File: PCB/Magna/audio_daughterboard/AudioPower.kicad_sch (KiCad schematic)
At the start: 54 parts, among them U901 TLV61046ADBVR, U902 TLV76701DRVx, U903 TLV76701DRVx, U904 TLV76701DRVx

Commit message: "Finalize" Audio daugherboard
Finished DAC output filter
Fixed the whole damn MCU subschematic
Fixed Linedriver schematic
Added component footprints and LCSC numbers
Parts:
- removed R901: 680R, Resistor_SMD:R_0805_2012Metric_Pad1.20x1.40mm_HandSolder, symbol Device:R_Small
- removed R904: 1k, Resistor_SMD:R_0805_2012Metric_Pad1.20x1.40mm_HandSolder, symbol Device:R_Small
- removed R911, R912: 470, Resistor_SMD:R_0805_2012Metric_Pad1.20x1.40mm_HandSolder, symbol Device:R_Small
- removed R913: 680, Resistor_SMD:R_0805_2012Metric_Pad1.20x1.40mm_HandSolder, symbol Device:R_Small
- removed U902, U903, U904: TLV76701DRVx, Package_SON:WSON-6-1EP_2x2mm_P0.65mm_EP1x1.6mm_ThermalVias, symbol Regulator_Linear:TLV76701DRVx
- added C904, C905, C906: 10uF, Capacitor_SMD:CP_Elec_4x5.8, symbol Device:C_Polarized
- added R901, R920: 680R, Resistor_SMD:R_0603_1608Metric, symbol Device:R
- added R904, R921: 2k15, Resistor_SMD:R_0603_1608Metric, symbol Device:R
- added R907, R911, R913: 22k, Resistor_SMD:R_0603_1608Metric, symbol Device:R
- added R912, R915: 10k, Resistor_SMD:R_0603_1608Metric, symbol Device:R
- added R914, R918: 100k, Resistor_SMD:R_0603_1608Metric, symbol Device:R
- added R916: 4k7, Resistor_SMD:R_0603_1608Metric, symbol Device:R
- added R919: 348R, Resistor_SMD:R_0603_1608Metric, symbol Device:R
- added TP902: TestPoint, TestPoint:TestPoint_Keystone_5005-5009_Compact, symbol Connector:TestPoint
- added U902, U903, U904: LM350_TO263-3, Package_TO_SOT_SMD:TO-263-3_TabPin2, symbol Regulator_Linear:LM350_TO220
- C901, C903, FB901, FB902, FB903, FB904, FB905, L901, R902, TP901, V901, V902: now left out of the parts list
- C902: footprint Capacitor_SMD:C_0805_2012Metric_Pad1.18x1.45mm_HandSolder -> Capacitor_SMD:C_0603_1608Metric; LCSC C1804 -> C1653; now left out of the parts list
- C907: renamed from C904; now left out of the parts list
- C908: renamed from C905; now left out of the parts list
- C909: renamed from C906; now left out of the parts list
- C910: renamed from C908; footprint (none) -> Capacitor_SMD:C_0603_1608Metric; LCSC (none) -> C1653; now left out of the parts list
- C911: renamed from C909; footprint (none) -> Capacitor_SMD:C_0603_1608Metric; LCSC (none) -> C1653; now left out of the parts list
- C912: renamed from C907; footprint (none) -> Capacitor_SMD:C_0603_1608Metric; LCSC (none) -> C1653; now left out of the parts list
- C913: renamed from C910; now left out of the parts list
- C914: renamed from C911; now left out of the parts list
- C915: renamed from C912; now left out of the parts list
- C916: renamed from C913; footprint Capacitor_SMD:CP_Elec_5x5.8 -> Skrooter_footprints:c_elec_SMD_12.5x13.5; symbol Device:C_Polarized -> Device:C; LCSC C2163245 -> C3829328; now left out of the parts list
- C917: renamed from C914; footprint Capacitor_SMD:CP_Elec_5x5.8 -> Skrooter_footprints:c_elec_SMD_12.5x13.5; symbol Device:C_Polarized -> Device:C; LCSC C2163245 -> C3829328; now left out of the parts list
- C918: renamed from C915; footprint Capacitor_SMD:CP_Elec_5x5.8 -> Skrooter_footprints:c_elec_SMD_12.5x13.5; symbol Device:C_Polarized -> Device:C; LCSC C2163245 -> C3829328; now left out of the parts list
- C919: renamed from C916; now left out of the parts list
- C920: renamed from C917; now left out of the parts list
- C921: renamed from C918; now left out of the parts list
- D901, D902, D903, D904, D905: footprint Diode_SMD:D_0805_2012Metric_Pad1.15x1.40mm_HandSolder -> LED_SMD:LED_0805_2012Metric; now left out of the parts list
- R903: footprint Resistor_SMD:R_0805_2012Metric_Pad1.20x1.40mm_HandSolder -> Resistor_SMD:R_0603_1608Metric; LCSC C149504 -> C95204; now left out of the parts list
- R905: value 499k -> 100k; footprint (none) -> Resistor_SMD:R_0603_1608Metric; LCSC (none) -> C25803; now left out of the parts list
- R906: value 160k -> 10k; footprint (none) -> Resistor_SMD:R_0603_1608Metric; LCSC (none) -> C95204; now left out of the parts list
- R908: value 33k -> 4k7; footprint (none) -> Resistor_SMD:R_0603_1608Metric; LCSC (none) -> C2989582; now left out of the parts list
- R909: value 160k -> 22k; footprint (none) -> Resistor_SMD:R_0603_1608Metric; LCSC (none) -> C335085; now left out of the parts list
- R910: value 15k -> 100k; footprint (none) -> Resistor_SMD:R_0603_1608Metric; LCSC (none) -> C25803; now left out of the parts list
- R917: renamed from R907; footprint (none) -> Resistor_SMD:R_0603_1608Metric; LCSC (none) -> C25803; now left out of the parts list
- TP903: renamed from TP902; now left out of the parts list
- TP904: renamed from TP903; now left out of the parts list
- TP905: renamed from TP904; now left out of the parts list
- TP906: renamed from TP905; now left out of the parts list
- TP907: renamed from TP906; now left out of the parts list
- U901: LCSC (none) -> C464815
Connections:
- net +5V: now also R901.2
- net 16V: now also C904.1, C905.1, C906.1, R904.2
- net Boost in: now also U902.3 (VI)
- net GND: now also C904.2, C905.2, C906.2, R913.2, R914.2, R916.1, R918.2, TP902.1; no longer R906.2, R908.2
- net 14.5VAA: now reaches C911.1, C915.1, C918.1, FB905.1
- net 14.5VAA: now also R905.1, R921.2, U904.2 (VO); no longer R909.1
- net at C910.1, C914.1, C917.1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: now also R920.2, U903.2 (VO)
- net at C910.2, R917.2: now also R910.1, R914.1, R918.1, U903.1 (ADJ); no longer R908.1
- net at C912.1, C913.1, C916.1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: now also R906.1, R919.2, U902.2 (VO); no longer R905.1
- net at C908.1, C909.1, FB902.2: now also U903.3 (VI), U904.3 (VI)
- net at D901.2 (A): now also R901.1
- net at D905.2 (A): now also R921.1
- net at D904.2 (A): now also R920.1
- net at D902.2 (A): now also R904.1
- net at D903.2 (A): now also R919.1
- new net: R905.2, R907.2
- new net: C912.2, R911.2, R913.1, U902.1 (ADJ)
- new net: R907.1, R909.2
- new net: C911.2, R912.2, R915.1, U904.1 (ADJ)
- new net: R909.1, R912.1
- new net: R915.2, R916.2
- new net: R906.2, R908.2
- new net: R908.1, R911.1
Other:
- note added: "Should be 36k over 22k"
- moved on the sheet: C902, C903, C907, C908, C909, C910, C911, C912, C913, C914, C915, C919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

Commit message: Do most of the component placement for audio board
Just a general layout, things will probably change
as the routing begins.
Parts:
- removed C905: 10uF, Capacitor_SMD:CP_Elec_4x5.8, symbol Device:C_Polarized
- removed C907, C913, C919: 4.7uF, Capacitor_SMD:C_0805_2012Metric_Pad1.18x1.45mm_HandSolder, symbol Device:C
- removed C912: 22pF, Capacitor_SMD:C_0603_1608Metric, symbol Device:C
- removed C916, C917, C918: 22uF, Skrooter_footprints:c_elec_SMD_12.5x13.5, symbol Device:C
- removed D903: Red, LED_SMD:LED_0805_2012Metric, symbol Device:LED_Small
- removed FB903: FerriteBead, Inductor_SMD:L_0805_2012Metric, symbol Device:FerriteBead
- removed R906: 10k, Resistor_SMD:R_0603_1608Metric, symbol Device:R
- removed R908: 4k7, Resistor_SMD:R_0603_1608Metric, symbol Device:R
- removed R911, R913: 22k, Resistor_SMD:R_0603_1608Metric, symbol Device:R
- removed R919: 348R, Resistor_SMD:R_0603_1608Metric, symbol Device:R
- removed TP901, TP904, TP905: TestPoint, TestPoint:TestPoint_Keystone_5005-5009_Compact, symbol Connector:TestPoint
- removed U902: LM350_TO263-3, Package_TO_SOT_SMD:TO-263-3_TabPin2, symbol Regulator_Linear:LM350_TO220
- added C913, C914, C917: 220uF, Capacitor_SMD:CP_Elec_4x5.8, symbol Device:C_Polarized
- added FB902: FerriteBead, Inductor_SMD:L_0805_2012Metric, symbol Device:FerriteBead
- added R903: 22k, Resistor_SMD:R_0603_1608Metric, symbol Device:R
- added TP1: TestPoint, TestPoint:TestPoint_Pad_1.0x1.0mm, symbol Connector:TestPoint_Alt
- added TP906, TP908: TestPoint, TestPoint:TestPoint_Keystone_5005-5009_Compact, symbol Connector:TestPoint
- C901, C903: footprint Capacitor_SMD:C_0805_2012Metric_Pad1.18x1.45mm_HandSolder -> Capacitor_SMD:C_1206_3216Metric; LCSC C1779 -> C29823
- C907: renamed from C908; footprint Capacitor_SMD:C_0805_2012Metric_Pad1.18x1.45mm_HandSolder -> Capacitor_SMD:C_1206_3216Metric; LCSC C1779 -> C29823
- C908: renamed from C909; footprint Capacitor_SMD:C_0805_2012Metric_Pad1.18x1.45mm_HandSolder -> Capacitor_SMD:C_1206_3216Metric; LCSC C1779 -> C29823
- C911: renamed from C914; footprint Capacitor_SMD:C_0805_2012Metric_Pad1.18x1.45mm_HandSolder -> Capacitor_SMD:C_1206_3216Metric; LCSC C1779 -> C29823
- C912: renamed from C915; footprint Capacitor_SMD:C_0805_2012Metric_Pad1.18x1.45mm_HandSolder -> Capacitor_SMD:C_1206_3216Metric; LCSC C1779 -> C29823
- C915: renamed from C920; footprint Capacitor_SMD:C_0805_2012Metric_Pad1.18x1.45mm_HandSolder -> Capacitor_SMD:C_1206_3216Metric; LCSC C1779 -> C29823
- C916: renamed from C921; footprint Capacitor_SMD:C_0805_2012Metric_Pad1.18x1.45mm_HandSolder -> Capacitor_SMD:C_1206_3216Metric; LCSC C1779 -> C29823
- R902: value 120k -> 100k; footprint Resistor_SMD:R_0805_2012Metric_Pad1.20x1.40mm_HandSolder -> Resistor_SMD:R_0603_1608Metric; LCSC C17709 -> C25803
- renumbered C910 to C909, C911 to C910, D904 to D903, D905 to D904, FB902 to FB903, R903 to R904, R904 to R905, R905 to R906, R910 to R907, R907 to R908, R914 to R910, R912 to R911, R917 to R912, R918 to R913, R915 to R914, R916 to R915, R920 to R916, R921 to R917, TP907 to TP905, TP906 to TP907, U903 to U902, U904 to U903
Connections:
- net +5VA: no longer TP907.1
- net 14.5VAA: now also TP905.1, C914.1
- net 16V: now also C917.1, FB902.1
- net Boost Feedback: now also R903.1; no longer R902.2
- net Boost_SW: now also TP1.1
- net GND: now also C913.2, C914.2, C917.2, TP906.1, TP908.1
- net VAA: no longer TP905.1
- net 5VA_PRE_FERRITE: now reaches C909.1, C911.1, FB904.1, R912.1, R916.2, U902.2 (VO)
- net 5VA_PRE_FERRITE: now also TP907.1, C913.1
- net at C908.1, FB903.2, U903.3 (VI): no longer C907.1, U902.3 (VI)
- net 14.5VAA_FEEDBACK: now reaches C910.2, R911.2, R914.1, U903.1 (ADJ)
- new net: R902.2, R903.2
- new net: C907.1, FB902.2, U902.3 (VI)
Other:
- note removed: "3.3V/250mA"
- note removed: "Should be 36k over 22k"
- moved on the sheet: C904, C907, C908, C909, C910, C911, C912, C915, C916, D903, D904, FB904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

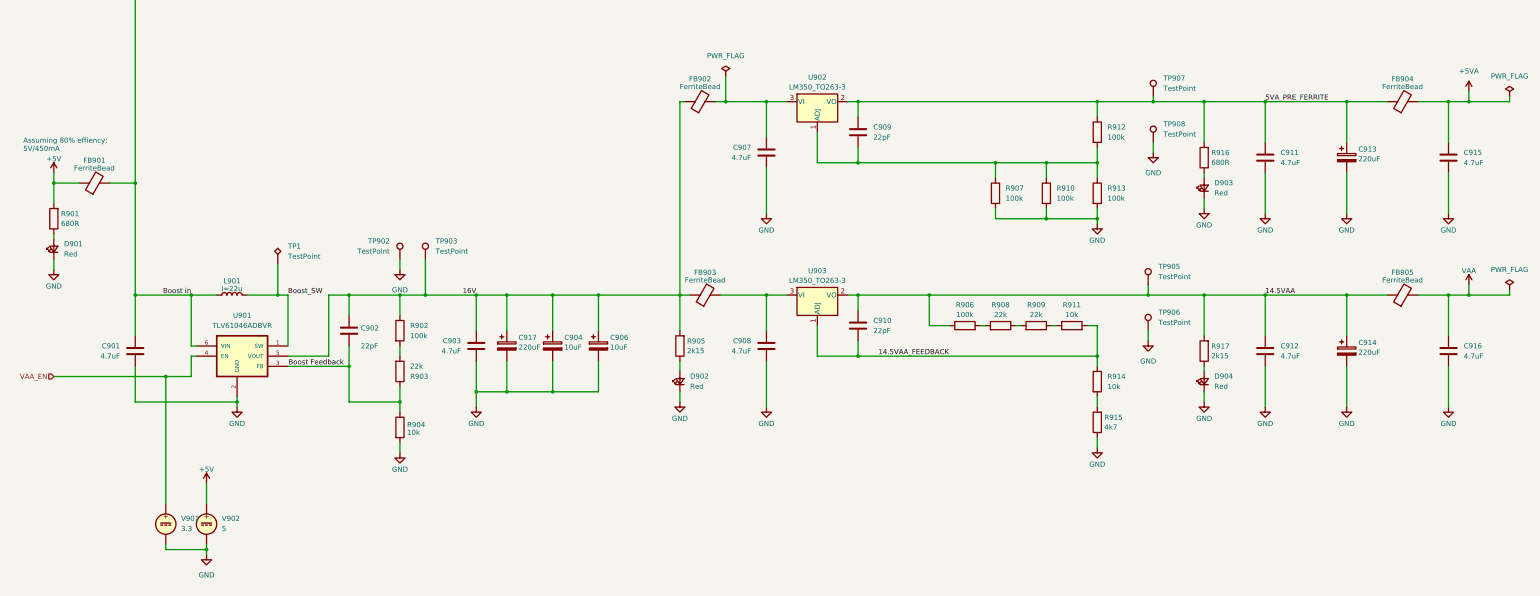
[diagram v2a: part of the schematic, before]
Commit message: Start layout and routing of Audio Daugherboard
Also a lot of small changes to everything that became apperant
when the audio daughterboard was designed. Such as the Headphone
PCB, which is now separate from the rest of the audio.
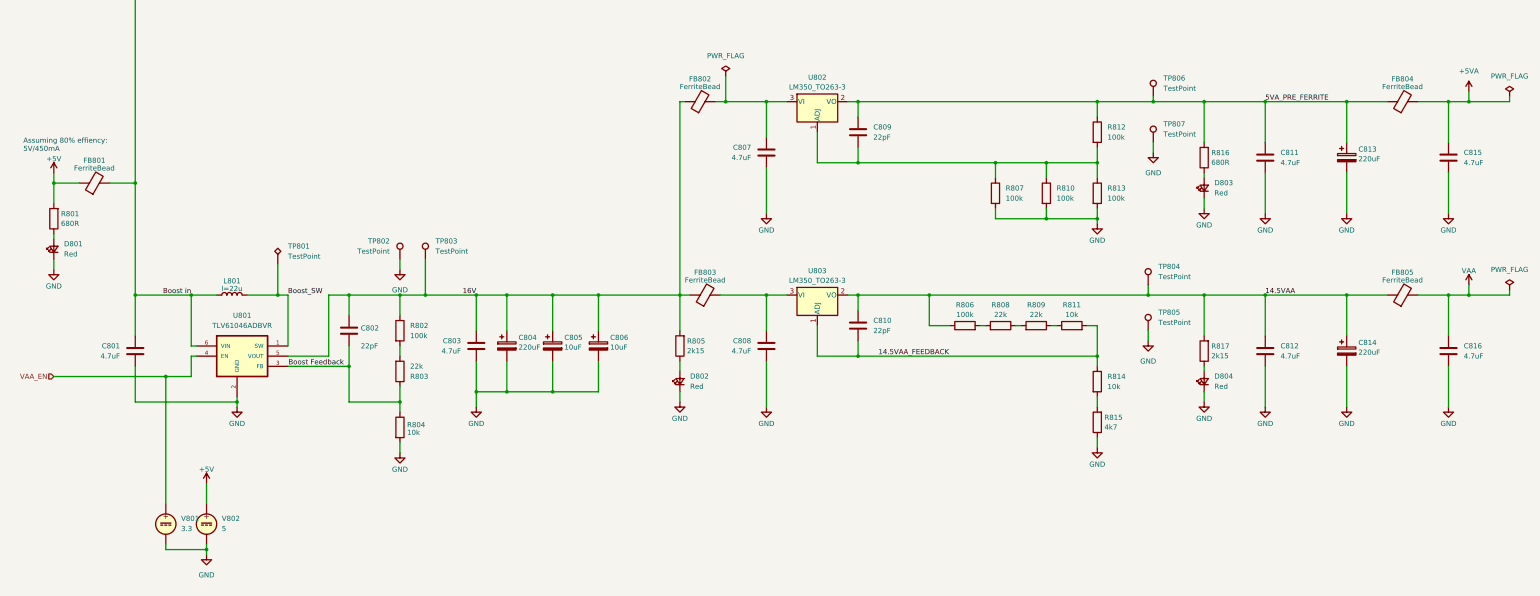
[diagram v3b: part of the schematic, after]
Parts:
- renumbered C901 to C801, C902 to C802, C903 to C803, C917 to C804, C904 to C805, C906 to C806, C907 to C807, C908 to C808, C909 to C809, C910 to C810, C911 to C811, C912 to C812, C913 to C813, C914 to C814, C915 to C815, C916 to C816, D901 to D801, D902 to D802, D903 to D803, D904 to D804, FB901 to FB801, FB902 to FB802, FB903 to FB803, FB904 to FB804, FB905 to FB805, L901 to L801, R901 to R801, R902 to R802, R903 to R803, R904 to R804, R905 to R805, R906 to R806, R907 to R807, R908 to R808, R909 to R809, R910 to R810, R911 to R811, R912 to R812, R913 to R813, R914 to R814, R915 to R815, R916 to R816, R917 to R817, TP1 to TP801, TP902 to TP802, TP903 to TP803, TP905 to TP804, TP906 to TP805, TP907 to TP806, TP908 to TP807, U901 to U801, U902 to U802, U903 to U803, V901 to V801, V902 to V802

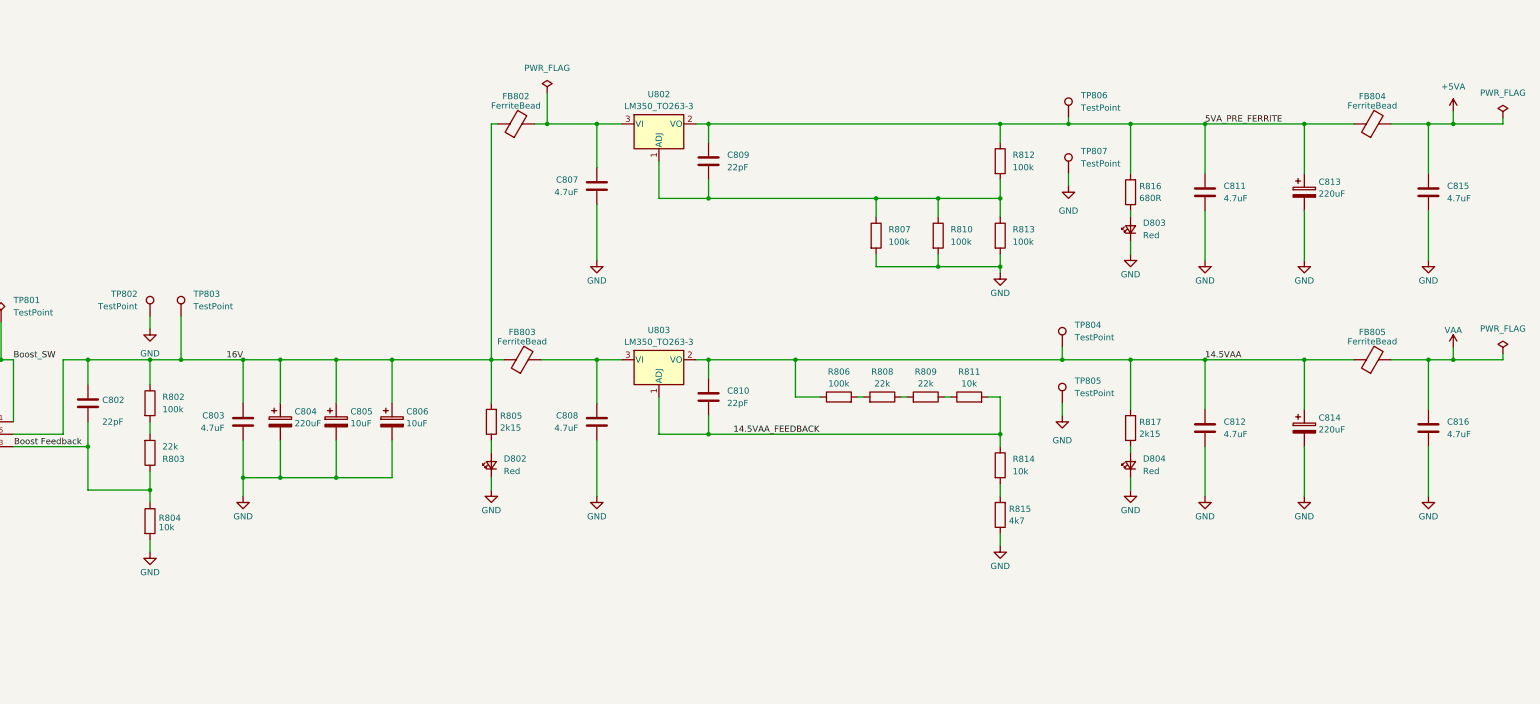
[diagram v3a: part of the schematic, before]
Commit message: Finished first round of routing for the Audio Daughterboard
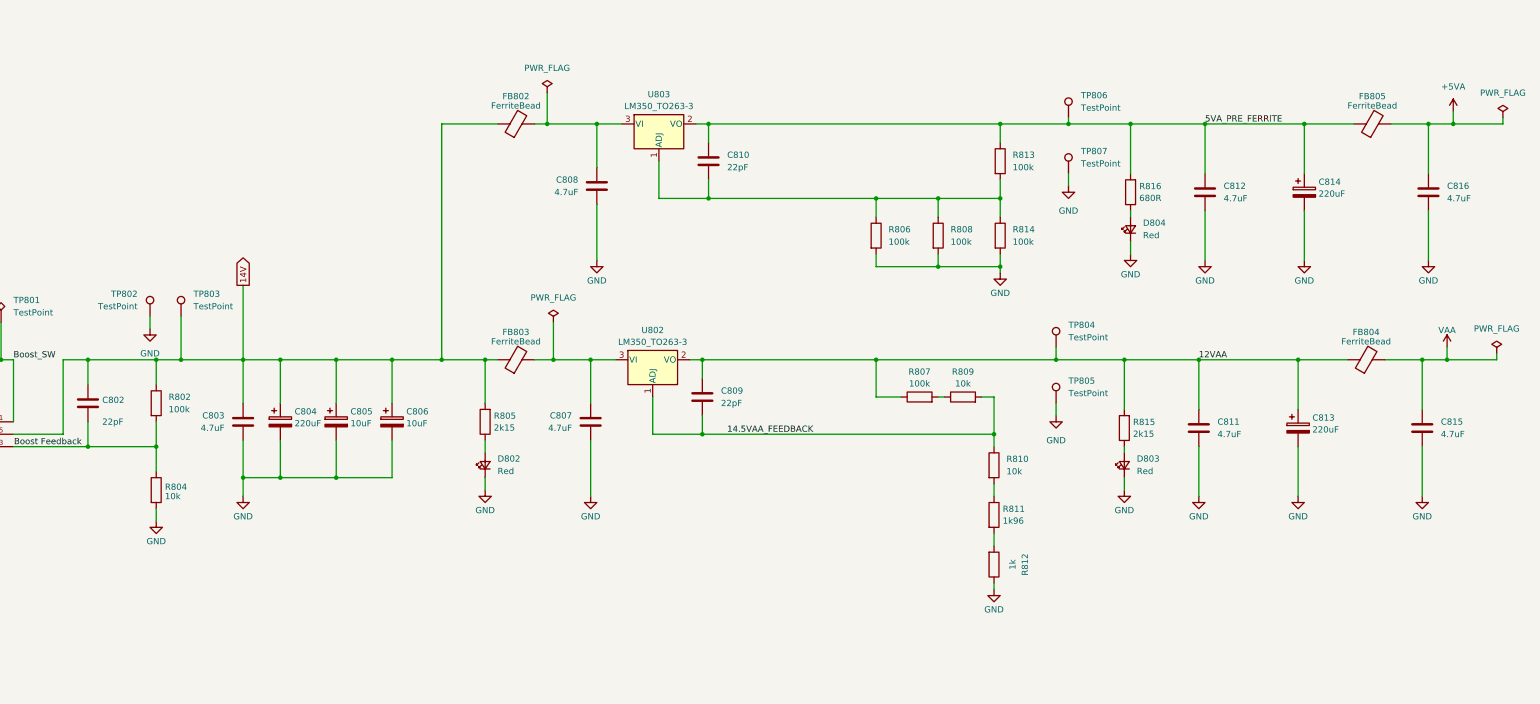
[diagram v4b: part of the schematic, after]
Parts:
- removed FB805: FerriteBead, Inductor_SMD:L_0805_2012Metric, symbol Device:FerriteBead
- removed R803, R808, R809: 22k, Resistor_SMD:R_0603_1608Metric, symbol Device:R
- removed R815: 4k7, Resistor_SMD:R_0603_1608Metric, symbol Device:R
- added FB804: FerriteBead, Inductor_SMD:L_0805_2012Metric, symbol Device:FerriteBead
- added R811: 1k96, Resistor_SMD:R_0603_1608Metric, symbol Device:R
- added R812: 1k, Resistor_SMD:R_0603_1608Metric, symbol Device:R
- R801, R816: LCSC C218116 -> C2989042; now in the parts list
- R802, R804, R805: now in the parts list
- R806: renamed from R807; now in the parts list
- R807: renamed from R806; now in the parts list
- R808: renamed from R810; now in the parts list
- R809: renamed from R811; now in the parts list
- R810: renamed from R814; now in the parts list
- R813: renamed from R812; now in the parts list
- R814: renamed from R813; now in the parts list
- R815: renamed from R817; now in the parts list
- renumbered C808 to C807, C807 to C808, C810 to C809, C809 to C810, C812 to C811, C811 to C812, C814 to C813, C813 to C814, C816 to C815, C815 to C816, D804 to D803, D803 to D804, FB804 to FB805, U803 to U802, U802 to U803
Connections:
- net Boost Feedback: now also R802.2
- net GND: now also R812.1
- net VAA: now also FB804.2
- net at R807.2: now also R809.1
- net at R810.2: now also R811.1
- net 14.5VAA renamed 12VAA
- net 12VAA: now also FB804.1
- net 16V renamed 14V
- new net: R811.2, R812.2
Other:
- moved on the sheet: C807, C809, C811, C813, C815, D802, D803, FB803, R802, R804, R805, R807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
